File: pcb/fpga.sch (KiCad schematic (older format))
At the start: 29 parts, among them J1 CONN_INTEGRALSTICK_FPGA_DEVICE, Q1 SSM6N58NU, Q2 SSM6N58NU, Q3 SSM6N58NU, U12 DSC6001HI2A-025.0000‎, U2 XC7A50T-1FTG256C, U9 AT24MAC402-UDFN

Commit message: Assigned lots of footprints. Still have a few to go.
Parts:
- C106, C44: footprint (none) -> azonenberg_pcb:EIA_0402_CAP_NOSILK
- D1, D3, D4, D5, D6: footprint (none) -> azonenberg_pcb:EIA_0603_LED
- Q1, Q2, Q3, R14, R15, R16, R17, R18, R19, R20, R27, R46, R47, R48, R49, R50, R61: footprint (none) -> azonenberg_pcb:EIA_0402_RES_NOSILK
- TP1: footprint (none) -> azonenberg_pcb:TESTPOINT_SMT_0.5MM
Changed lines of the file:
@@
 F 0 "U9" H 3850 9497 60  0000 C CNN
 F 1 "AT24MAC402-UDFN" H 3850 9391 60  0000 C CNN
-F 2 "" H 3850 9000 60  0000 C CNN
+F 2 "" H 3850 9000 60  0001 C CNN
 F 3 "" H 3850 9000 60  0000 C CNN
 	1    3450 8700
@@
 F 0 "C44" H 2765 8146 50  0000 L CNN
 F 1 "0.47 uF" H 2765 8055 50  0000 L CNN
-F 2 "" H 2688 7950 50  0001 C CNN
+F 2 "azonenberg_pcb:EIA_0402_CAP_NOSILK" H 2688 7950 50  0001 C CNN
 F 3 "" H 2650 8100 50  0001 C CNN
 	1    2650 8100
@@
 F 0 "R14" H 5070 8046 50  0000 L CNN
 F 1 "4.7k" H 5070 7955 50  0000 L CNN
-F 2 "" V 4930 8000 50  0001 C CNN
+F 2 "azonenberg_pcb:EIA_0402_RES_NOSILK" V 4930 8000 50  0001 C CNN
 F 3 "" H 5000 8000 50  0001 C CNN
 	1    5000 8000
@@
 F 0 "R15" H 5420 8046 50  0000 L CNN
 F 1 "4.7k" H 5420 7955 50  0000 L CNN
-F 2 "" V 5280 8000 50  0001 C CNN
+F 2 "azonenberg_pcb:EIA_0402_RES_NOSILK" V 5280 8000 50  0001 C CNN
 F 3 "" H 5350 8000 50  0001 C CNN
 	1    5350 8000
@@
 F 0 "R16" H 7620 3146 50  0000 L CNN
 F 1 "100" H 7620 3055 50  0000 L CNN
-F 2 "" V 7480 3100 50  0001 C CNN
+F 2 "azonenberg_pcb:EIA_0402_RES_NOSILK" V 7480 3100 50  0001 C CNN
 F 3 "" H 7550 3100 50  0001 C CNN
 	1    7550 3100
@@
 F 0 "Q1" H 11343 8103 60  0000 L CNN
 F 1 "SSM6N58NU" H 11343 7997 60  0000 L CNN
-F 2 "" H 11200 8050 60  0000 C CNN
+F 2 "azonenberg_pcb:EIA_0402_RES_NOSILK" H 11200 8050 60  0001 C CNN
 F 3 "" H 11343 7944 60  0000 L CNN
 	1    11200 8050
@@
 F 0 "D1" V 11139 7582 50  0000 R CNN
 F 1 "GREEN" V 11048 7582 50  0000 R CNN
-F 2 "" H 11100 7700 50  0001 C CNN
+F 2 "azonenberg_pcb:EIA_0603_LED" H 11100 7700 50  0001 C CNN
 F 3 "" H 11100 7700 50  0001 C CNN
 	1    11100 7700
@@
 F 0 "R17" H 11170 7446 50  0000 L CNN
 F 1 "470" H 11170 7355 50  0000 L CNN
-F 2 "" V 11030 7400 50  0001 C CNN
+F 2 "azonenberg_pcb:EIA_0402_RES_NOSILK" V 11030 7400 50  0001 C CNN
 F 3 "" H 11100 7400 50  0001 C CNN
 	1    11100 7400
@@
 F 0 "R20" V 13050 5350 50  0000 C CNN
 F 1 "4.7k" V 13000 5150 50  0000 C CNN
-F 2 "" V 12930 5150 50  0001 C CNN
+F 2 "azonenberg_pcb:EIA_0402_RES_NOSILK" V 12930 5150 50  0001 C CNN
 F 3 "" H 13000 5150 50  0001 C CNN
 	1    13000 5150
@@
 F 0 "R19" V 13050 5250 50  0000 C CNN
 F 1 "4.7k" V 13000 5050 50  0000 C CNN
-F 2 "" V 12930 5050 50  0001 C CNN
+F 2 "azonenberg_pcb:EIA_0402_RES_NOSILK" V 12930 5050 50  0001 C CNN
 F 3 "" H 13000 5050 50  0001 C CNN
 	1    13000 5050
@@
 F 0 "R18" V 13050 5150 50  0000 C CNN
 F 1 "1K" V 13000 4950 50  0000 C CNN
-F 2 "" V 12930 4950 50  0001 C CNN
+F 2 "azonenberg_pcb:EIA_0402_RES_NOSILK" V 12930 4950 50  0001 C CNN
 F 3 "" H 13000 4950 50  0001 C CNN
 	1    13000 4950
@@
 F 0 "TP1" H 12667 7825 50  0000 C CNN
 F 1 "TESTPAD" H 12667 7916 50  0000 C CNN
-F 2 "" H 12750 8050 50  0001 C CNN
+F 2 "azonenberg_pcb:TESTPOINT_SMT_0.5MM" H 12750 8050 50  0001 C CNN
 F 3 "" H 12750 8050 50  0001 C CNN
 	1    12750 8050
@@
 F 0 "U12" H 3825 7387 60  0000 C CNN
 F 1 "DSC6001HI2A-025.0000‎" H 3825 7281 60  0000 C CNN
-F 2 "" H 3850 7100 60  0000 C CNN
+F 2 "" H 3850 7100 60  0001 C CNN
 F 3 "" H 3850 7100 60  0000 C CNN
 	1    3850 7100
@@
 F 0 "R27" V 4650 7000 50  0000 C CNN
 F 1 "33" V 4750 7100 50  0000 C CNN
-F 2 "" V 4680 7100 50  0001 C CNN
+F 2 "azonenberg_pcb:EIA_0402_RES_NOSILK" V 4680 7100 50  0001 C CNN
 F 3 "" H 4750 7100 50  0001 C CNN
 	1    4750 7100
@@
 F 0 "C106" H 2515 7196 50  0000 L CNN
 F 1 "0.47 uF" H 2515 7105 50  0000 L CNN
-F 2 "" H 2438 7000 50  0001 C CNN
+F 2 "azonenberg_pcb:EIA_0402_CAP_NOSILK" H 2438 7000 50  0001 C CNN
 F 3 "" H 2400 7150 50  0001 C CNN
 	1    2400 7150
@@
 F 0 "Q2" H 5993 10303 60  0000 L CNN
 F 1 "SSM6N58NU" H 5993 10197 60  0000 L CNN
-F 2 "" H 5850 10250 60  0000 C CNN
+F 2 "azonenberg_pcb:EIA_0402_RES_NOSILK" H 5850 10250 60  0001 C CNN
 F 3 "" H 5993 10144 60  0000 L CNN
 	1    5850 10250
@@
 F 0 "R46" H 5820 9646 50  0000 L CNN
 F 1 "470" H 5820 9555 50  0000 L CNN
-F 2 "" V 5680 9600 50  0001 C CNN
+F 2 "azonenberg_pcb:EIA_0402_RES_NOSILK" V 5680 9600 50  0001 C CNN
 F 3 "" H 5750 9600 50  0001 C CNN
 	1    5750 9600
@@
 F 0 "D3" V 5789 9782 50  0000 R CNN
 F 1 "GREEN" V 5698 9782 50  0000 R CNN
-F 2 "" H 5750 9900 50  0001 C CNN
+F 2 "azonenberg_pcb:EIA_0603_LED" H 5750 9900 50  0001 C CNN
 F 3 "" H 5750 9900 50  0001 C CNN
 	1    5750 9900
@@
 F 0 "Q2" H 7143 10303 60  0000 L CNN
 F 1 "SSM6N58NU" H 7143 10197 60  0000 L CNN
-F 2 "" H 7000 10250 60  0000 C CNN
+F 2 "azonenberg_pcb:EIA_0402_RES_NOSILK" H 7000 10250 60  0001 C CNN
 F 3 "" H 7143 10144 60  0000 L CNN
 	2    7000 10250
@@
 F 0 "R47" H 6970 9646 50  0000 L CNN
 F 1 "470" H 6970 9555 50  0000 L CNN
-F 2 "" V 6830 9600 50  0001 C CNN
+F 2 "azonenberg_pcb:EIA_0402_RES_NOSILK" V 6830 9600 50  0001 C CNN
 F 3 "" H 6900 9600 50  0001 C CNN
 	1    6900 9600
@@
 F 0 "D4" V 6939 9782 50  0000 R CNN
 F 1 "GREEN" V 6848 9782 50  0000 R CNN
-F 2 "" H 6900 9900 50  0001 C CNN
+F 2 "azonenberg_pcb:EIA_0603_LED" H 6900 9900 50  0001 C CNN
 F 3 "" H 6900 9900 50  0001 C CNN
 	1    6900 9900
@@
 F 0 "Q3" H 8393 10303 60  0000 L CNN
 F 1 "SSM6N58NU" H 8393 10197 60  0000 L CNN
-F 2 "" H 8250 10250 60  0000 C CNN
+F 2 "azonenberg_pcb:EIA_0402_RES_NOSILK" H 8250 10250 60  0001 C CNN
 F 3 "" H 8393 10144 60  0000 L CNN
 	1    8250 10250
@@
 F 0 "R48" H 8220 9646 50  0000 L CNN
 F 1 "470" H 8220 9555 50  0000 L CNN
-F 2 "" V 8080 9600 50  0001 C CNN
+F 2 "azonenberg_pcb:EIA_0402_RES_NOSILK" V 8080 9600 50  0001 C CNN
 F 3 "" H 8150 9600 50  0001 C CNN
 	1    8150 9600
@@
 F 0 "D5" V 8189 9782 50  0000 R CNN
 F 1 "GREEN" V 8098 9782 50  0000 R CNN
-F 2 "" H 8150 9900 50  0001 C CNN
+F 2 "azonenberg_pcb:EIA_0603_LED" H 8150 9900 50  0001 C CNN
 F 3 "" H 8150 9900 50  0001 C CNN
 	1    8150 9900
@@
 F 0 "Q3" H 9543 10303 60  0000 L CNN
 F 1 "SSM6N58NU" H 9543 10197 60  0000 L CNN
-F 2 "" H 9400 10250 60  0000 C CNN
+F 2 "azonenberg_pcb:EIA_0402_RES_NOSILK" H 9400 10250 60  0001 C CNN
 F 3 "" H 9543 10144 60  0000 L CNN
 	2    9400 10250
@@
 F 0 "R49" H 9370 9646 50  0000 L CNN
 F 1 "470" H 9370 9555 50  0000 L CNN
-F 2 "" V 9230 9600 50  0001 C CNN
+F 2 "azonenberg_pcb:EIA_0402_RES_NOSILK" V 9230 9600 50  0001 C CNN
 F 3 "" H 9300 9600 50  0001 C CNN
 	1    9300 9600
@@
 F 0 "D6" V 9339 9782 50  0000 R CNN
 F 1 "GREEN" V 9248 9782 50  0000 R CNN
-F 2 "" H 9300 9900 50  0001 C CNN
+F 2 "azonenberg_pcb:EIA_0603_LED" H 9300 9900 50  0001 C CNN
 F 3 "" H 9300 9900 50  0001 C CNN
 	1    9300 9900
@@
 F 0 "R50" V 13800 4950 50  0000 C CNN
 F 1 "33" V 13750 4750 50  0000 C CNN
-F 2 "" V 13680 4750 50  0001 C CNN
+F 2 "azonenberg_pcb:EIA_0402_RES_NOSILK" V 13680 4750 50  0001 C CNN
 F 3 "" H 13750 4750 50  0001 C CNN
 	1    13750 4750
@@
 F 0 "R61" V 13550 4550 50  0000 C CNN
 F 1 "33" V 13500 4350 50  0000 C CNN
-F 2 "" V 13430 4350 50  0001 C CNN
+F 2 "azonenberg_pcb:EIA_0402_RES_NOSILK" V 13430 4350 50  0001 C CNN
 F 3 "" H 13500 4350 50  0001 C CNN
 	1    13500 4350

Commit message: Assigned inductor footprints
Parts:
- Q1, Q2, Q3: footprint azonenberg_pcb:EIA_0402_RES_NOSILK -> azonenberg_pcb:DFN_6_0.65MM_2x2MM_GDS
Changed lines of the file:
@@
 F 0 "Q1" H 11343 8103 60  0000 L CNN
 F 1 "SSM6N58NU" H 11343 7997 60  0000 L CNN
-F 2 "azonenberg_pcb:EIA_0402_RES_NOSILK" H 11200 8050 60  0001 C CNN
+F 2 "azonenberg_pcb:DFN_6_0.65MM_2x2MM_GDS" H 11200 8050 60  0001 C CNN
 F 3 "" H 11343 7944 60  0000 L CNN
 	1    11200 8050
@@
 F 0 "Q2" H 5993 10303 60  0000 L CNN
 F 1 "SSM6N58NU" H 5993 10197 60  0000 L CNN
-F 2 "azonenberg_pcb:EIA_0402_RES_NOSILK" H 5850 10250 60  0001 C CNN
+F 2 "azonenberg_pcb:DFN_6_0.65MM_2x2MM_GDS" H 5850 10250 60  0001 C CNN
 F 3 "" H 5993 10144 60  0000 L CNN
 	1    5850 10250
@@
 F 0 "Q2" H 7143 10303 60  0000 L CNN
 F 1 "SSM6N58NU" H 7143 10197 60  0000 L CNN
-F 2 "azonenberg_pcb:EIA_0402_RES_NOSILK" H 7000 10250 60  0001 C CNN
+F 2 "azonenberg_pcb:DFN_6_0.65MM_2x2MM_GDS" H 7000 10250 60  0001 C CNN
 F 3 "" H 7143 10144 60  0000 L CNN
 	2    7000 10250
@@
 F 0 "Q3" H 8393 10303 60  0000 L CNN
 F 1 "SSM6N58NU" H 8393 10197 60  0000 L CNN
-F 2 "azonenberg_pcb:EIA_0402_RES_NOSILK" H 8250 10250 60  0001 C CNN
+F 2 "azonenberg_pcb:DFN_6_0.65MM_2x2MM_GDS" H 8250 10250 60  0001 C CNN
 F 3 "" H 8393 10144 60  0000 L CNN
 	1    8250 10250
@@
 F 0 "Q3" H 9543 10303 60  0000 L CNN
 F 1 "SSM6N58NU" H 9543 10197 60  0000 L CNN
-F 2 "azonenberg_pcb:EIA_0402_RES_NOSILK" H 9400 10250 60  0001 C CNN
+F 2 "azonenberg_pcb:DFN_6_0.65MM_2x2MM_GDS" H 9400 10250 60  0001 C CNN
 F 3 "" H 9543 10144 60  0000 L CNN
 	2    9400 10250

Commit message: Finished initial footprint assignments
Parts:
- U12: footprint (none) -> azonenberg_pcb:OSCILLATOR_1.6x1.2
- U9: footprint (none) -> azonenberg_pcb:DFN_8_0.5MM_2x3MM
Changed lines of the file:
@@
 F 0 "U9" H 3850 9497 60  0000 C CNN
 F 1 "AT24MAC402-UDFN" H 3850 9391 60  0000 C CNN
-F 2 "" H 3850 9000 60  0001 C CNN
+F 2 "azonenberg_pcb:DFN_8_0.5MM_2x3MM" H 3850 9000 60  0001 C CNN
 F 3 "" H 3850 9000 60  0000 C CNN
 	1    3450 8700
@@
 F 0 "U12" H 3825 7387 60  0000 C CNN
 F 1 "DSC6001HI2A-025.0000‎" H 3825 7281 60  0000 C CNN
-F 2 "" H 3850 7100 60  0001 C CNN
+F 2 "azonenberg_pcb:OSCILLATOR_1.6x1.2" H 3850 7100 60  0001 C CNN
 F 3 "" H 3850 7100 60  0000 C CNN
 	1    3850 7100

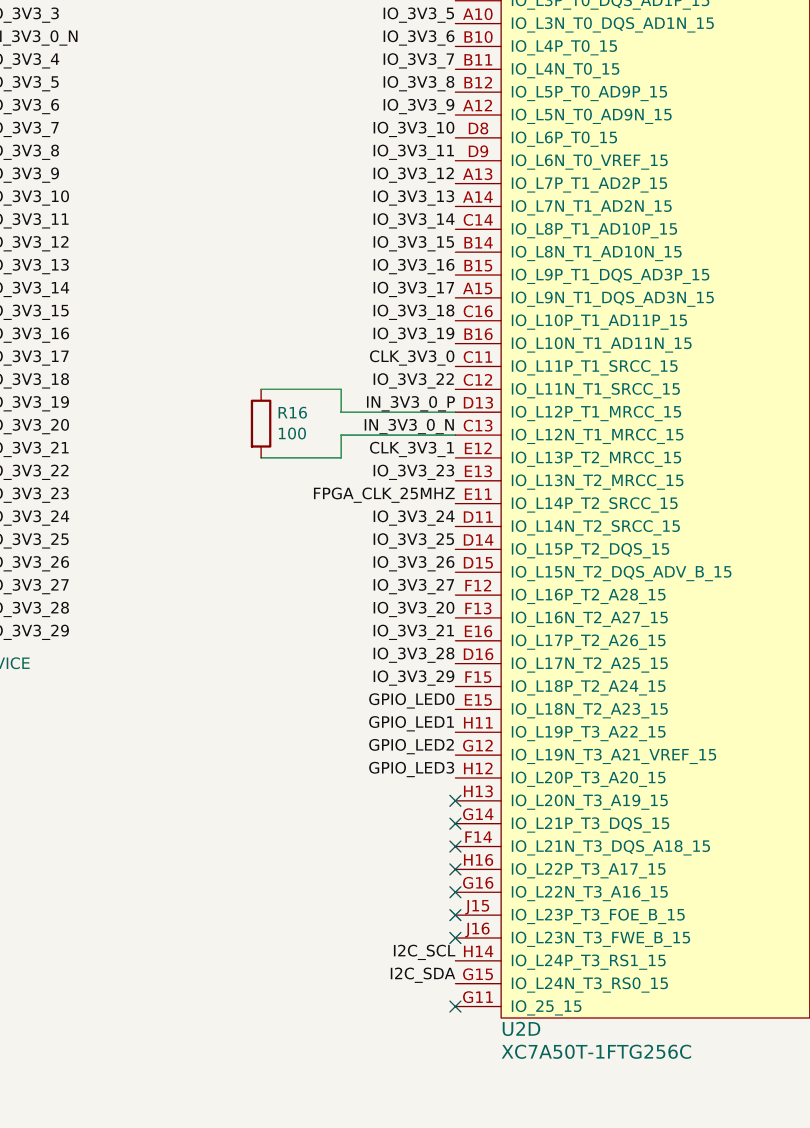
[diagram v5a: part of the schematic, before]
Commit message: Initial work on FPGA fanout
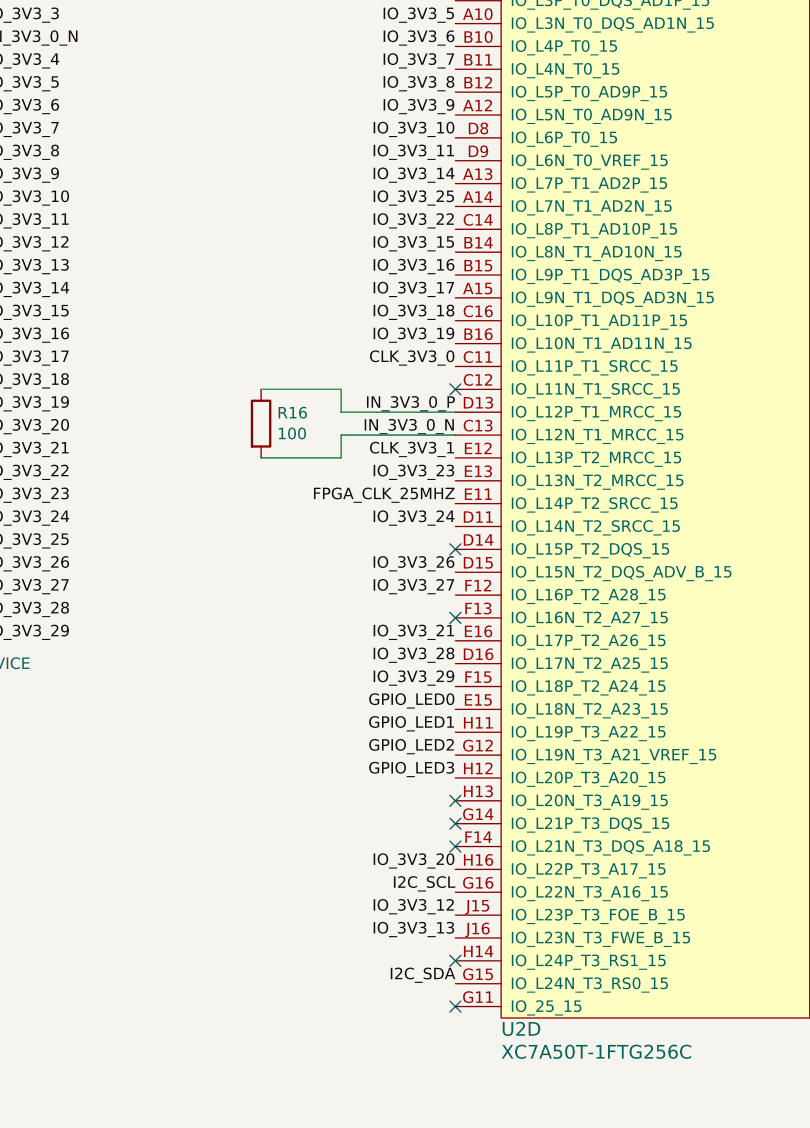
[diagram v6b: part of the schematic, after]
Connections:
- net I2C_SCL: now also U2.G16 (IO_L22N_T3_A16_15); no longer U2.H14 (IO_L24P_T3_RS1_15)
- net IO_3V3_12: now also U2.J15 (IO_L23P_T3_FOE_B_15); no longer U2.A13 (IO_L7P_T1_AD2P_15)
- net IO_3V3_13: now also U2.J16 (IO_L23N_T3_FWE_B_15); no longer U2.A14 (IO_L7N_T1_AD2N_15)
- net IO_3V3_14: now also U2.A13 (IO_L7P_T1_AD2P_15); no longer U2.C14 (IO_L8P_T1_AD10P_15)
- net IO_3V3_20: now also U2.H16 (IO_L22P_T3_A17_15); no longer U2.F13 (IO_L16N_T2_A27_15)
- net IO_3V3_22: now also U2.C14 (IO_L8P_T1_AD10P_15); no longer U2.C12 (IO_L11N_T1_SRCC_15)
- net IO_3V3_25: now also U2.A14 (IO_L7N_T1_AD2N_15); no longer U2.D14 (IO_L15P_T2_DQS_15)
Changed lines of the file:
@@
 Text Label 8400 1950 2    50   ~ 0
 IO_3V3_11
+Text Label 8400 5250 2    50   ~ 0
+IO_3V3_12
+Text Label 8400 5350 2    50   ~ 0
+IO_3V3_13
 Text Label 8400 2050 2    50   ~ 0
-IO_3V3_12
-Text Label 8400 2150 2    50   ~ 0
-IO_3V3_13
-Text Label 8400 2250 2    50   ~ 0
 IO_3V3_14
 Text Label 8400 2350 2    50   ~ 0
@@
 Text Label 8400 2750 2    50   ~ 0
 IO_3V3_19
-Text Label 8400 3950 2    50   ~ 0
+Text Label 8400 5050 2    50   ~ 0
 IO_3V3_20
 Text Label 8400 4050 2    50   ~ 0
 IO_3V3_21
-Text Label 8400 2950 2    50   ~ 0
+Text Label 8400 2250 2    50   ~ 0
 IO_3V3_22
 Text Label 8400 3350 2    50   ~ 0
@@
 Text Label 8400 3550 2    50   ~ 0
 IO_3V3_24
-Text Label 8400 3650 2    50   ~ 0
+Text Label 8400 2150 2    50   ~ 0
 IO_3V3_25
 Text Label 8400 3750 2    50   ~ 0
@@
 NoConn ~ 8400 4850
 NoConn ~ 8400 4950
-NoConn ~ 8400 5050
-NoConn ~ 8400 5150
-NoConn ~ 8400 5250
-NoConn ~ 8400 5350
 NoConn ~ 8400 5650
 $Comp
@@
 Wire Wire Line
 	5000 7850 5350 7850
-Text Label 8400 5450 2    50   ~ 0
+Text Label 8400 5150 2    50   ~ 0
 I2C_SCL
 Text Label 8400 5550 2    50   ~ 0
 I2C_SDA
-$Comp
-L xilinx-azonenberg:XC7AxT-xFTG256x U2
-U 4 1 5B8B9F8B
-P 8600 5650
-F 0 "U2" H 8600 5550 60  0000 L CNN
-F 1 "XC7A50T-1FTG256C" H 8600 5450 60  0000 L CNN
-F 2 "azonenberg_pcb:BGA_256_17x17_FULLARRAY_1MM" H 8600 5650 60  0001 C CNN
-F 3 "" H 8600 5650 60  0000 C CNN
-	4    8600 5650
-	1    0    0    -1
-$EndComp
 $Comp
 L device:R R16
@@
 Wire Wire Line
 	13650 4350 13900 4350
+NoConn ~ 8400 5450
+NoConn ~ 8400 3950
+NoConn ~ 8400 3650
+$Comp
+L xilinx-azonenberg:XC7AxT-xFTG256x U2
+U 4 1 5B8B9F8B
+P 8600 5650
+F 0 "U2" H 8600 5550 60  0000 L CNN
+F 1 "XC7A50T-1FTG256C" H 8600 5450 60  0000 L CNN
+F 2 "azonenberg_pcb:BGA_256_17x17_FULLARRAY_1MM" H 8600 5650 60  0001 C CNN
+F 3 "" H 8600 5650 60  0000 C CNN
+	4    8600 5650
+	1    0    0    -1
+$EndComp
+NoConn ~ 8400 2950
 $EndSCHEMATC

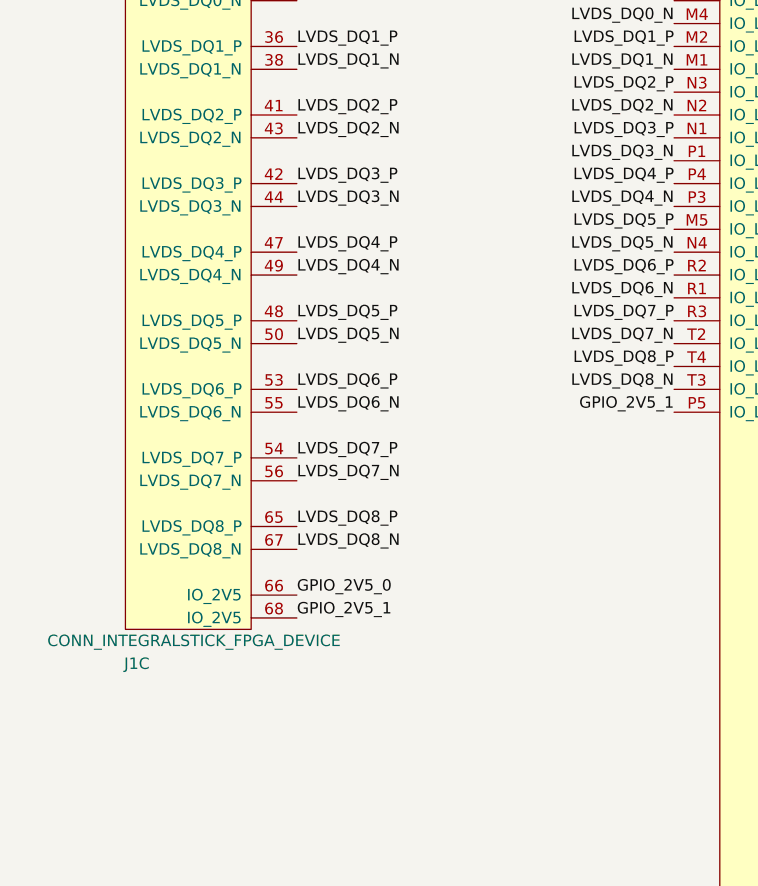
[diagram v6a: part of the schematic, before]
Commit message: Finished first iteration layout of RAM. Lots of pin swaps.
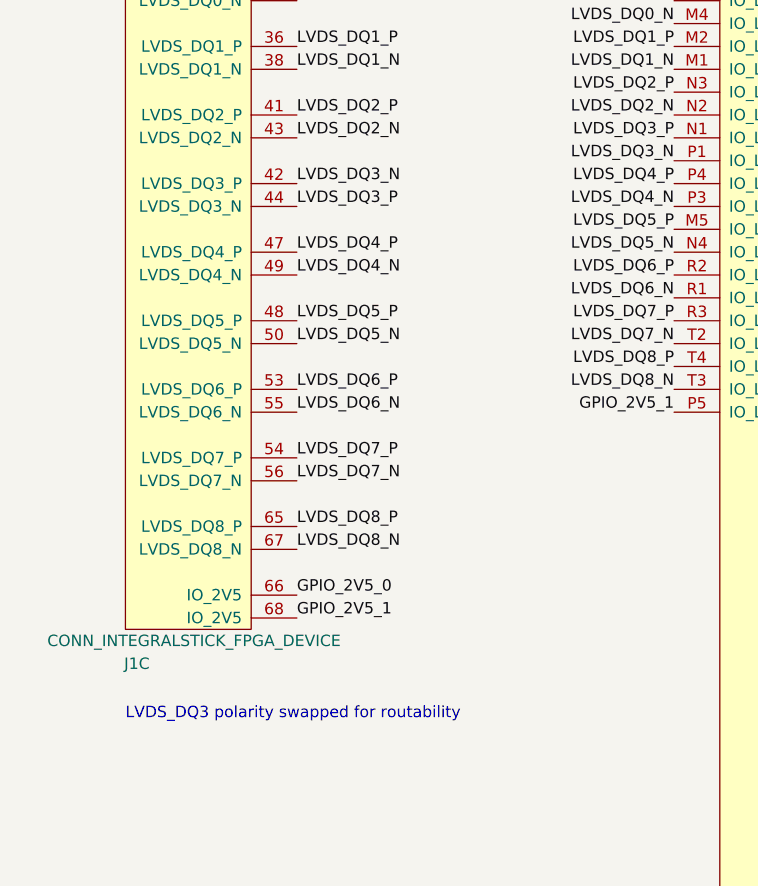
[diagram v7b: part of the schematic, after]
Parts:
- U2: footprint azonenberg_pcb:BGA_256_17x17_FULLARRAY_1MM -> azonenberg_pcb:BGA_256_17x17_FULLARRAY_1MM_0.4MM_FTG256
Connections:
- net LVDS_DQ3_N: now also J1.42 (LVDS_DQ3_P); no longer J1.44 (LVDS_DQ3_N)
- net LVDS_DQ3_P: now also J1.44 (LVDS_DQ3_N); no longer J1.42 (LVDS_DQ3_P)
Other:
- note added: "LVDS_DQ3 polarity swapped for routability"
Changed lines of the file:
@@
 Sheet 6 8
 Title "INTEGRALSTICK Compute Module"
-Date "2018-11-09"
+Date "2018-11-11"
 Rev "0.1"
 Comp "Andrew D. Zonenberg"
@@
 F 0 "U2" H 14100 5550 60  0000 L CNN
 F 1 "XC7A50T-1FTG256C" H 14100 5450 60  0000 L CNN
-F 2 "azonenberg_pcb:BGA_256_17x17_FULLARRAY_1MM" H 14100 5650 60  0001 C CNN
+F 2 "azonenberg_pcb:BGA_256_17x17_FULLARRAY_1MM_0.4MM_FTG256" H 14100 5650 60  0001 C CNN
 F 3 "" H 14100 5650 60  0000 C CNN
 	1    14100 5650
@@
 F 0 "U2" H 3500 5550 60  0000 L CNN
 F 1 "XC7A50T-1FTG256C" H 3500 5450 60  0000 L CNN
-F 2 "azonenberg_pcb:BGA_256_17x17_FULLARRAY_1MM" H 3500 5650 60  0001 C CNN
+F 2 "azonenberg_pcb:BGA_256_17x17_FULLARRAY_1MM_0.4MM_FTG256" H 3500 5650 60  0001 C CNN
 F 3 "" H 3500 5650 60  0000 C CNN
 	5    3500 5650
@@
 Text Label 1650 1450 0    50   ~ 0
 LVDS_DQ2_N
+Text Label 1650 1750 0    50   ~ 0
+LVDS_DQ3_P
 Text Label 1650 1650 0    50   ~ 0
-LVDS_DQ3_P
-Text Label 1650 1750 0    50   ~ 0
 LVDS_DQ3_N
 Text Label 1650 1950 0    50   ~ 0
@@
 F 0 "U2" H 8600 5550 60  0000 L CNN
 F 1 "XC7A50T-1FTG256C" H 8600 5450 60  0000 L CNN
-F 2 "azonenberg_pcb:BGA_256_17x17_FULLARRAY_1MM" H 8600 5650 60  0001 C CNN
+F 2 "azonenberg_pcb:BGA_256_17x17_FULLARRAY_1MM_0.4MM_FTG256" H 8600 5650 60  0001 C CNN
 F 3 "" H 8600 5650 60  0000 C CNN
 	4    8600 5650
@@
 $EndComp
 NoConn ~ 8400 2950
+Text Notes 900  4000 0    50   ~ 0
+LVDS_DQ3 polarity swapped for routability
 $EndSCHEMATC
